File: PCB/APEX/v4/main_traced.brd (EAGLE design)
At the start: 189 x 115.3 mm, 24 parts

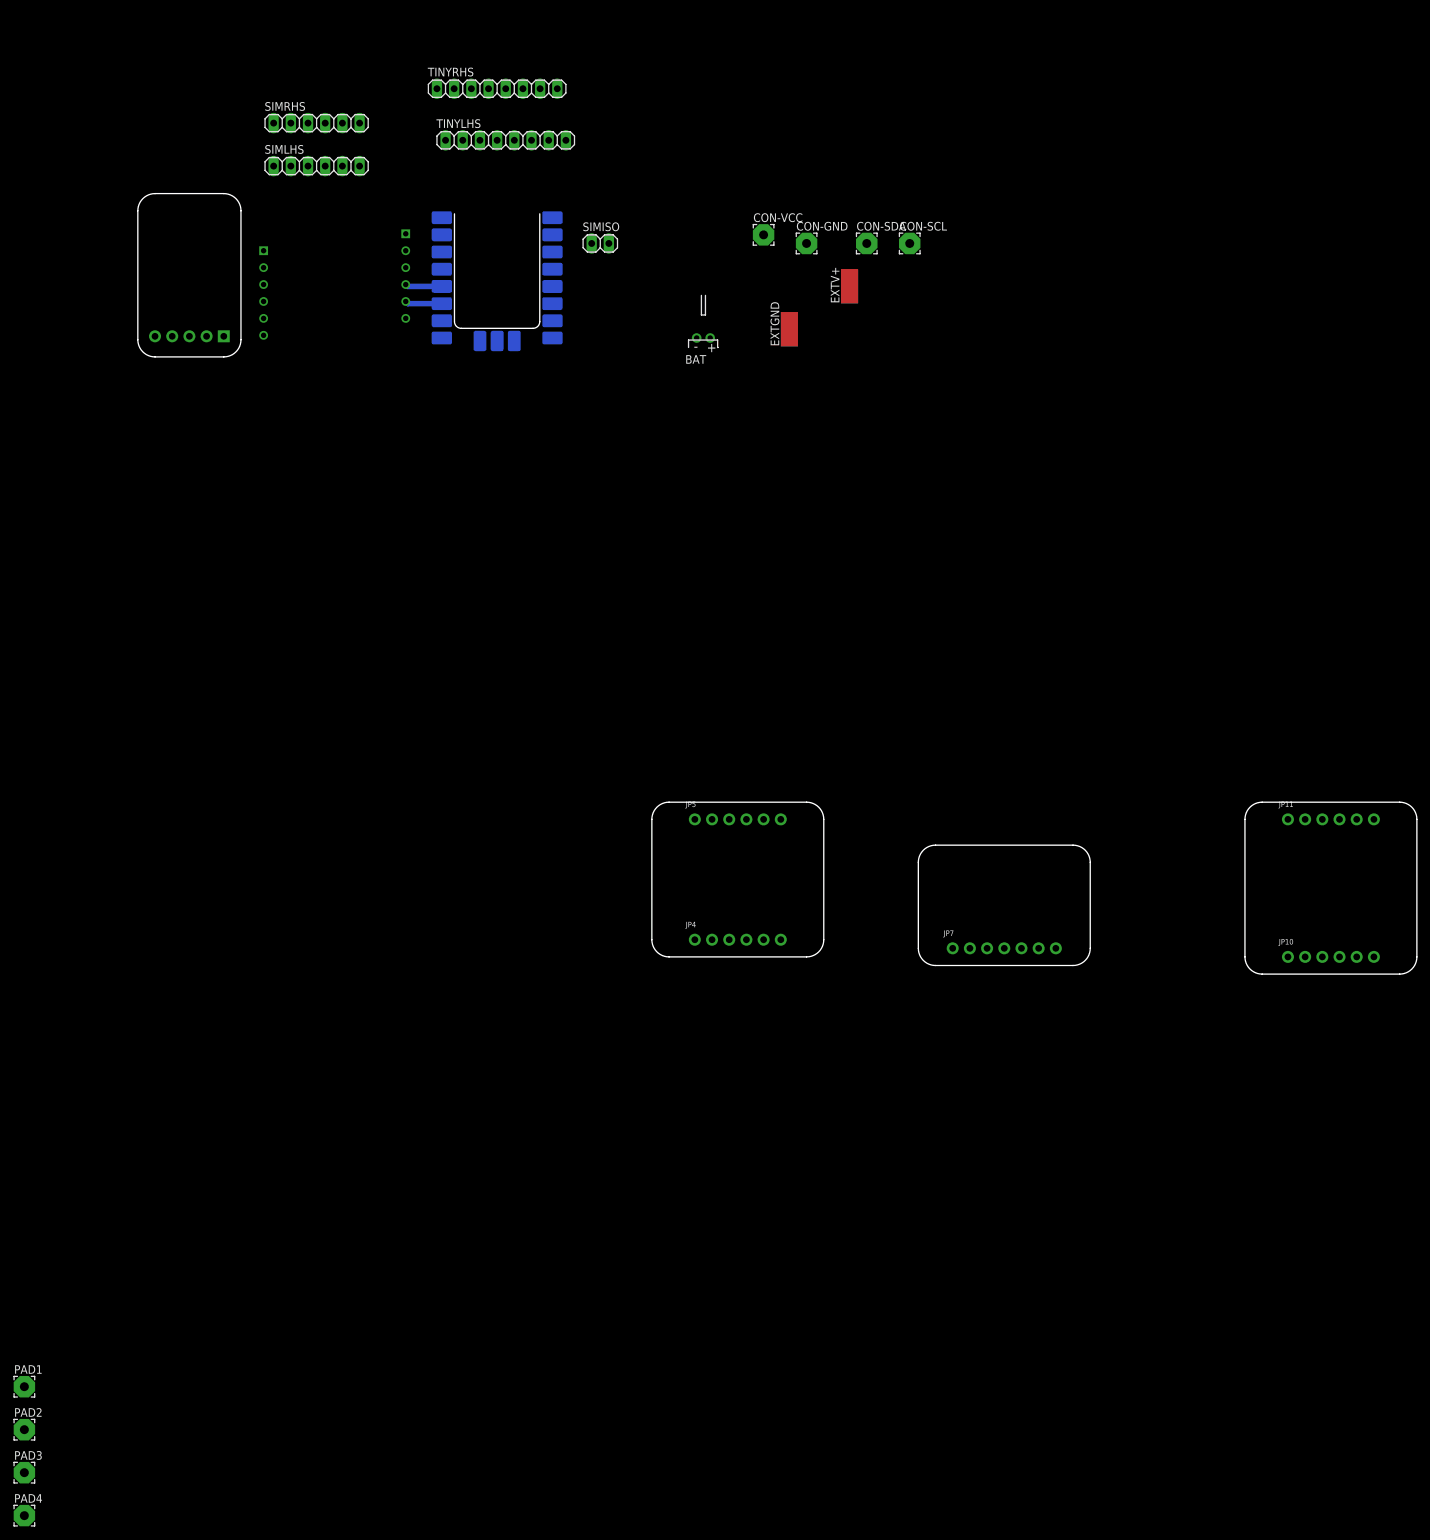
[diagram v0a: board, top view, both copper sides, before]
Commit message: replace tiny footprint with headers
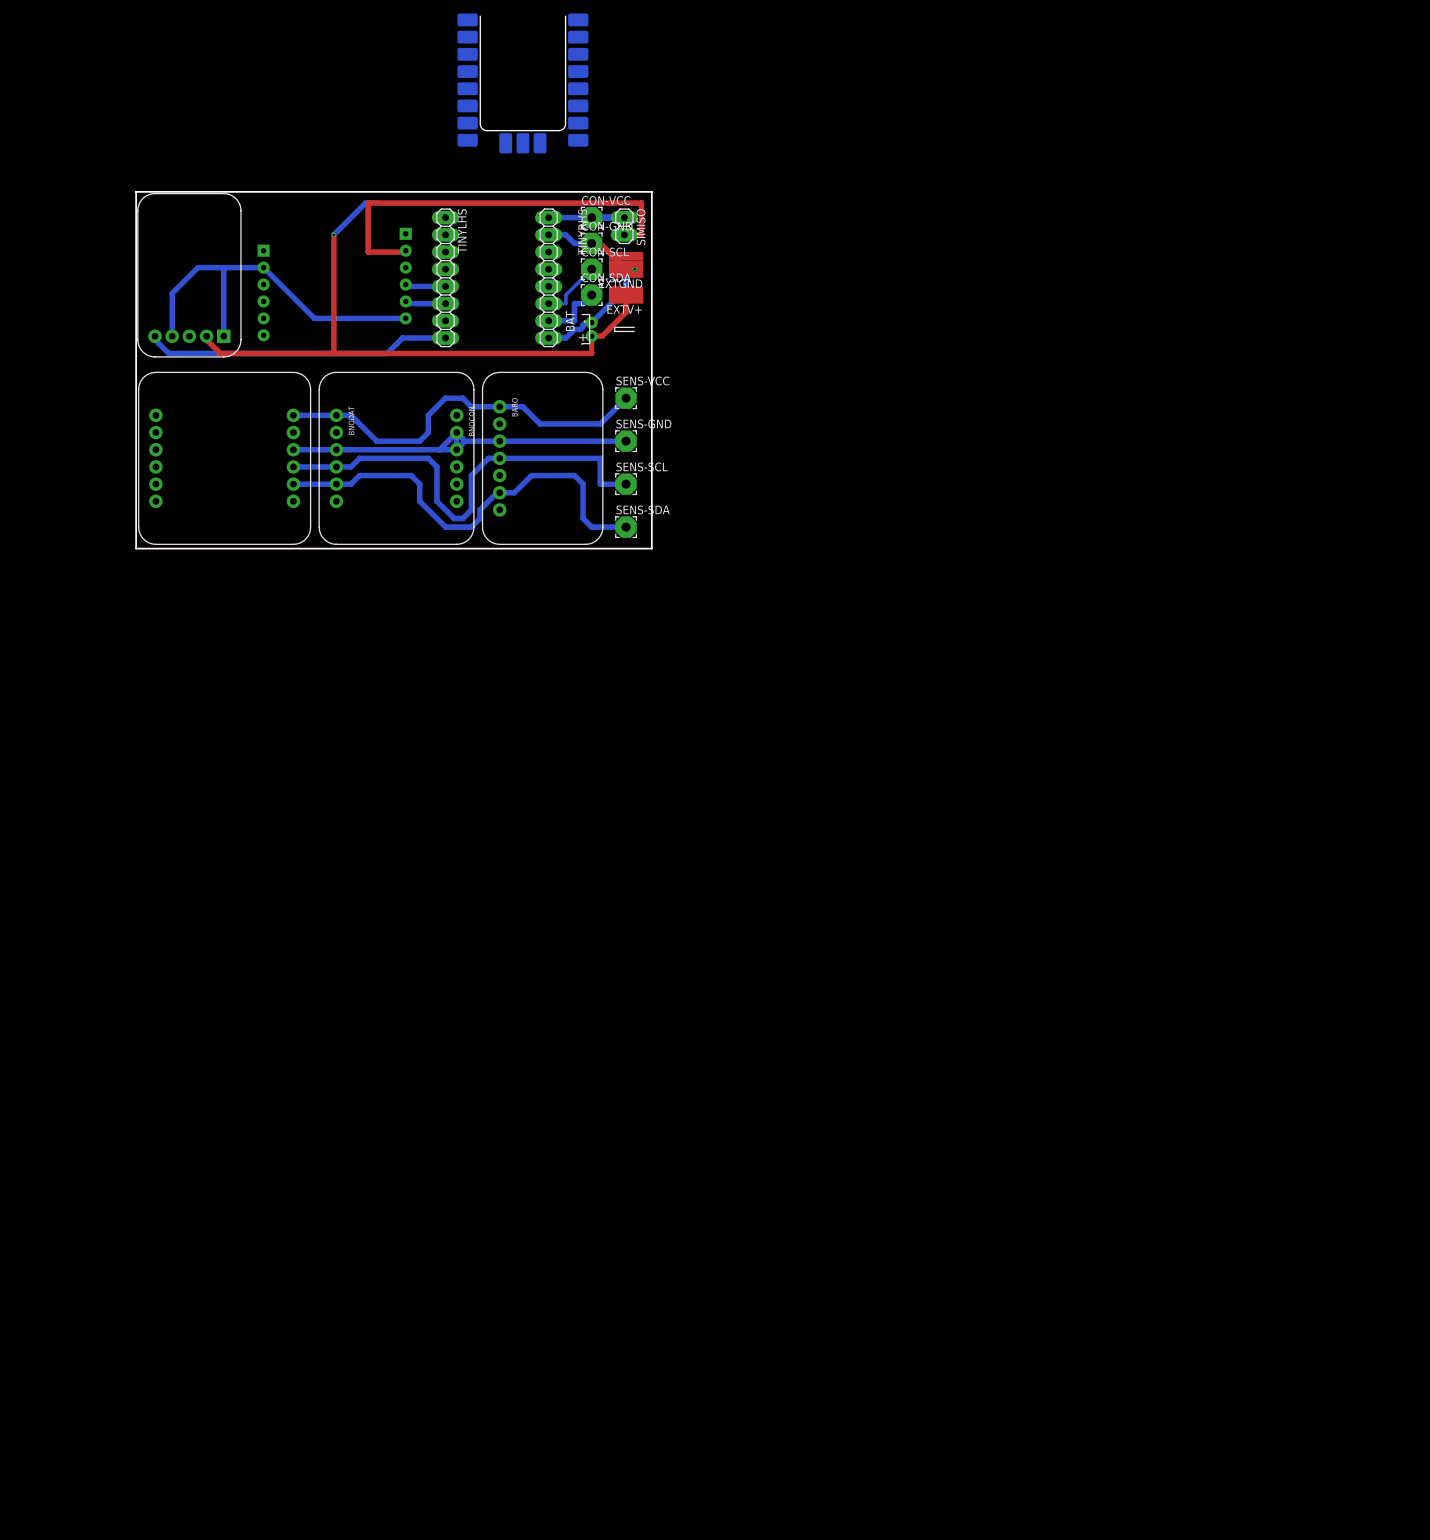
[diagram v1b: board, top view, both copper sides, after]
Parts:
- removed JP10, JP11, JP4, JP5: (no value), microbuilder:1X06_ROUND_70
- removed JP7: (no value), microbuilder:1X07_ROUND_70
- removed PAD1, PAD2, PAD3, PAD4: (no value), wirepad:3,17/1,3
- removed SIMLHS, SIMRHS: (no value), pinhead:1X06
- added BARO: (no value), microbuilder:1X07_ROUND_70
- added BNOCON, BNODAT, GPSDAT, GPSMOUNT: (no value), microbuilder:1X06_ROUND_70
- added SENS-GND, SENS-SCL, SENS-SDA, SENS-VCC: (no value), wirepad:3,17/1,3
- moved CON-SCL 47.1 mm to (68.6, 61.0)
- moved CON-SDA 41.3 mm to (68.6, 57.1)
- moved EXTV+ 33.0 mm to (73.7, 57.1), turned to 90 degrees
- moved CON-GND 31.8 mm to (68.6, 64.8)
- moved A1 29.5 mm to (58.4, 99.1)
- moved TINYRHS 29.0 mm to (62.2, 59.7), turned to 270 degrees
- moved EXTGND 25.7 mm to (73.7, 61.0), turned to 90 degrees
- moved CON-VCC 25.5 mm to (68.6, 68.6)
- moved TINYLHS 22.2 mm to (47.0, 59.7), turned to 270 degrees
- moved BAT 16.6 mm to (68.6, 52.1), turned to 270 degrees
- moved SIMISO 4.37 mm to (73.4, 67.3), turned to 270 degrees
- renumbered JP2 to AMP
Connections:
- net !RESET: now also GPSDAT.6; no longer JP10.6
- net 1PPS: now also GPSMOUNT.2; no longer JP11.2
- net 3.3V_2: now also BARO.2; no longer JP7.2
- net 3.3V_3: now also GPSDAT.2; no longer JP10.2
- net 3.3V_BNO: now also BNODAT.2; no longer JP4.2
- net AIN+: now also TINYLHS.8
- net BOOT: now also BNOCON.1; no longer JP5.1
- net CS: now also BNOCON.6; no longer JP5.6
- net CS_BARO: now also BARO.7; no longer JP7.7
- net GND: now also BARO.3, BNOCON.2, BNOCON.3, BNODAT.3, GPSDAT.3, GPSMOUNT.1, SENS-GND.1, TINYRHS.2, TINYRHS.8; no longer JP10.3, JP11.1, JP4.3, JP5.2, JP5.3, JP7.3, PAD2.1
- net INT: now also BNODAT.6; no longer JP4.6
- net MOSI: now also BNOCON.5; no longer JP5.5
- net RX: now also TINYLHS.5
- net RXI: now also GPSMOUNT.4; no longer JP11.4
- net SCL: now also BARO.4, BNODAT.4, GPSDAT.4, SENS-SCL.1, TINYRHS.6; no longer JP10.4, JP4.4, JP7.4, PAD3.1
- net SDA: now also BARO.6, BNODAT.5, GPSDAT.5, SENS-SDA.1, TINYRHS.7; no longer JP10.5, JP4.5, JP7.6, PAD4.1
- net SDO/ADR: now also BARO.5; no longer JP7.5
- net TX: now also TINYLHS.6
- net TXO: now also GPSMOUNT.5; no longer JP11.5
- net VCC: now also BARO.1, BNOCON.4, BNODAT.1, GPSDAT.1, GPSMOUNT.3, SENS-VCC.1, TINYRHS.1; no longer JP10.1, JP11.3, JP4.1, JP5.4, JP7.1, PAD1.1
- net WAKEUP: now also GPSMOUNT.6; no longer JP11.6
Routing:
- net VCC: track 0.00 -> 165.1 mm, vias 0 -> 1
- net GND: track 0.00 -> 145.6 mm, vias 0 -> 1
- net SCL: track 0.00 -> 76.0 mm
- net SDA: track 0.00 -> 73.8 mm
- net SIMPOW: track 0.00 -> 60.5 mm
- net AIN+: track 0.00 -> 45.2 mm
- net TX: track 5.46 -> 6.01 mm
- net RX: track 5.45 -> 6.00 mm
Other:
- board size 189 x 115.3 mm -> 76.2 x 52.7 mm

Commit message: labelling
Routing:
- net VCC: track 165.1 -> 191.2 mm
- net SDA: track 73.8 -> 72.3 mm
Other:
- board text added: "5V Top Right"
- board text added: "AIN+ AIN_ SD VCC GND"
- board text added: "AMP"
- board text added: "BARO"
- board text added: "BNO085"
- board text added: "BOOT P0 P1 RST MOSI CS"
- board text added: "GND"
- board text added: "GND 1PPS VCC RXI TXO WAKEUP"
- board text added: "GPS"
- board text added: "NET VCC RST RX TX GND"
- board text added: "RING DTR MIC+ MIC- SPK+ SPK-"
- board text added: "RX TX Unused AIN+"
- board text added: "SCL"
- board text added: "SCL SDA GND"
- board text added: "SDA"
- board text added: "SIM Isolation"
- board text added: "SIM800L"
- board text added: "Tiny 2040"
- board text added: "USB C Up"
- board text added: "VCC"
- board text added: "VCC 3V3 GND SCL SDA INT"
- board text added: "VCC 3V3 GND SCL SDA RST"
- board text added: "VCC 3V3 GND SCL SDO SDA CS"
- board text added: "VCC GND"
